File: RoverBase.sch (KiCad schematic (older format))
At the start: 64 parts, among them J1 Conn_01x01, J2 Conn_01x06, J3 Conn_01x04, J4 Conn_01x02, J5 Conn_01x03, J6 Conn_02x03_Counter_Clockwise, J7 Conn_02x03_Counter_Clockwise, J8 Conn_01x01, J9 Conn_01x06, SW1 SW_SPDT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

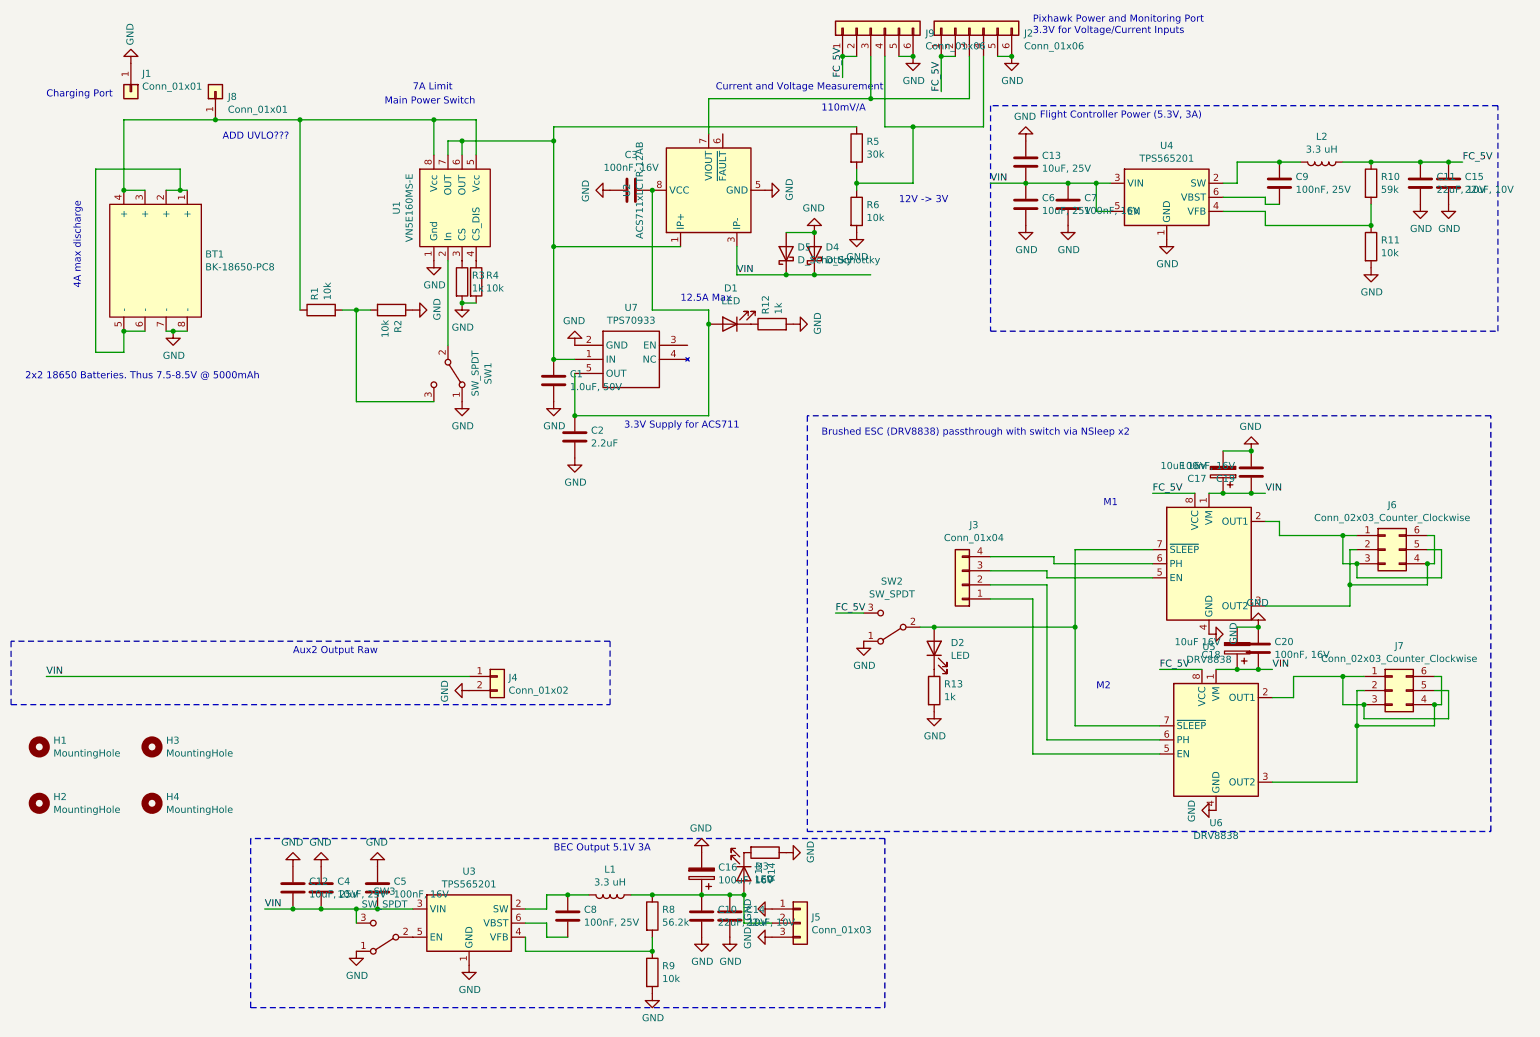
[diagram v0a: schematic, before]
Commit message: Remove diodes and add thermal via for motor controllers
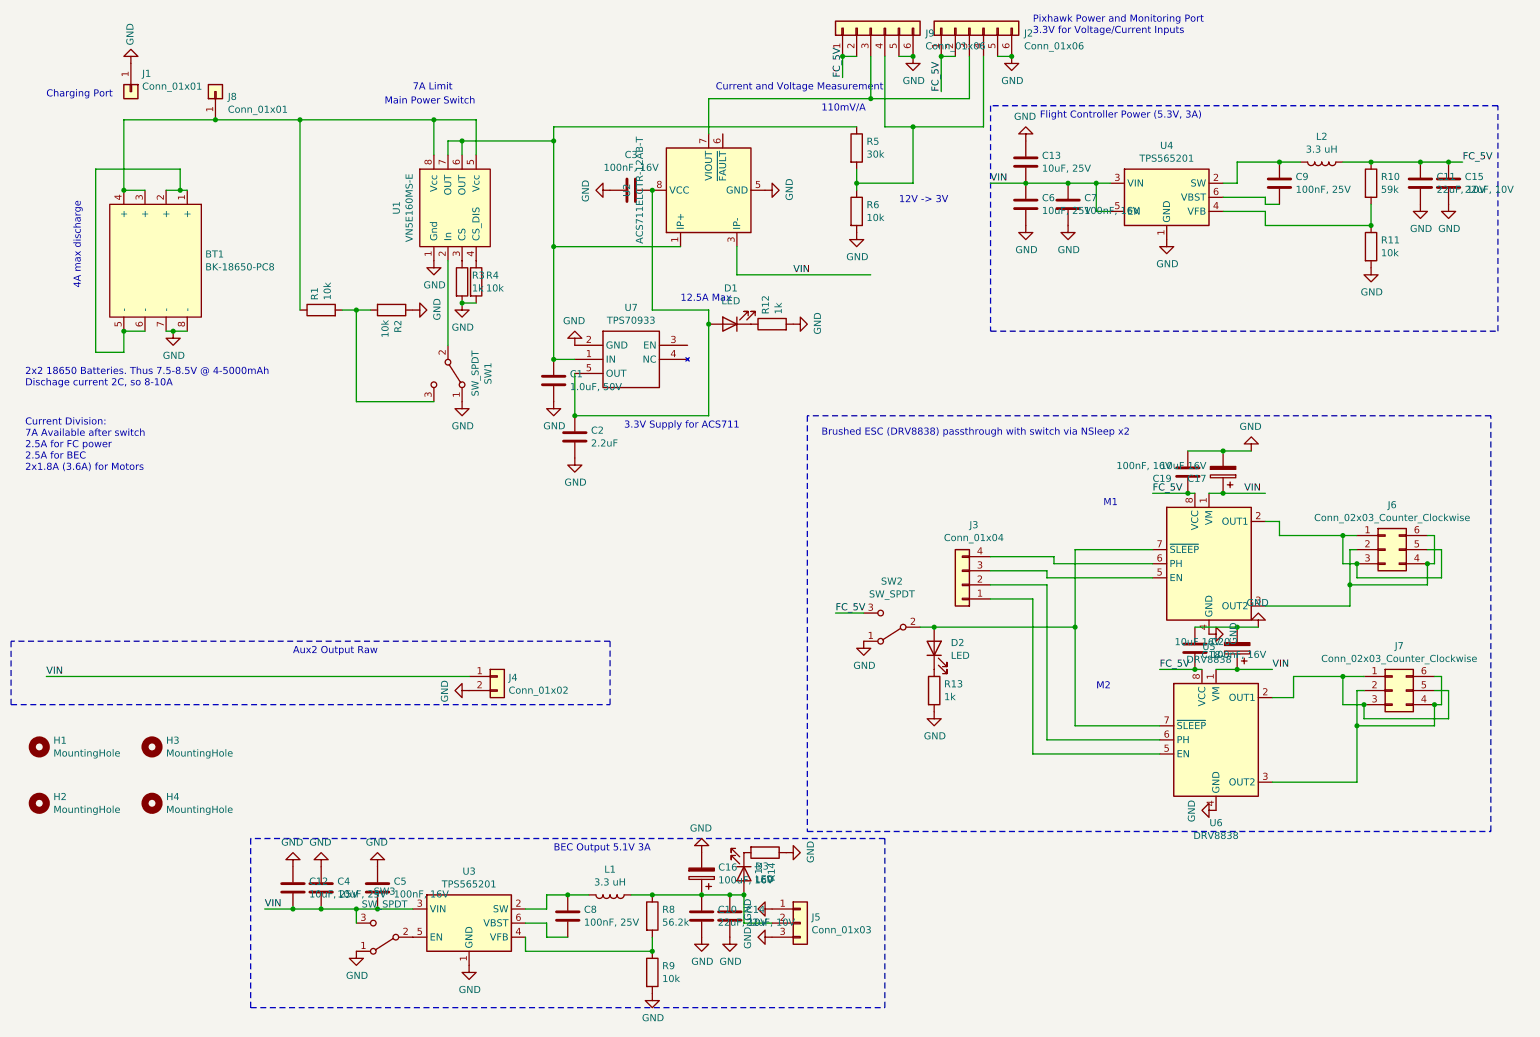
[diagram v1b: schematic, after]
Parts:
- removed D4, D5: D_Schottky, Diode_SMD:D_SOD-323, symbol Device:D_Schottky
- J6, J7: MPN PPPC032LFBN-RC -> nf; Manufacturer Sullins Connector Solutions -> nf; SPN S7106-ND -> nf; fit_field (none) -> dnf
- U2: value ACS711xLCTR-12AB -> ACS711ELCTR-12AB-T
- U5, U6: footprint Package_SON:WSON-8-1EP_2x2mm_P0.5mm_EP0.9x1.6mm -> Package_SON:WSON-8-1EP_2x2mm_P0.5mm_EP0.9x1.6mm_ThermalVias
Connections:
- net FC_5V: now also C19.1, C20.2
- net VIN: no longer C19.1, C20.2
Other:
- note added: "2x2 18650 Batteries. Thus 7.5-8.5V @ 4-5000mAh\nDischage current 2C, so 8-10A\n"
- note added: "Current Division:\n7A Available after switch\n2.5A for FC power\n2.5A for BEC\n2x1.8A (3.6A) for Motors"
- note removed: "2x2 18650 Batteries. Thus 7.5-8.5V @ 5000mAh"
- note removed: "ADD UVLO???"
- moved on the sheet: C19, C20
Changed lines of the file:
@@
 Text Notes 8350 5350 0    50   ~ 0
 M2
-Text Notes 750  3150 0    50   ~ 0
-2x2 18650 Batteries. Thus 7.5-8.5V @ 5000mAh
+Text Notes 750  3200 0    50   ~ 0
+2x2 18650 Batteries. Thus 7.5-8.5V @ 4-5000mAh\nDischage current 2C, so 8-10A\n
 Text Notes 900  1150 0    50   ~ 0
 Charging Port
@@
 P 5600 1800
 F 0 "U2" H 5600 2381 50  0000 C CNN
-F 1 "ACS711xLCTR-12AB" H 5600 2290 50  0000 C CNN
+F 1 "ACS711ELCTR-12AB-T" H 5600 2290 50  0000 C CNN
 F 2 "Package_SO:SOIC-8_3.9x4.9mm_P1.27mm" H 5950 1750 50  0001 L CIN
 F 3 "http://www.allegromicro.com/~/Media/Files/Datasheets/ACS711-Datasheet.ashx" H 5600 1800 50  0001 C CNN
@@
 Text Notes 7950 1300 0    50   ~ 0
 Flight Controller Power (5.3V, 3A)
-Wire Wire Line
-	5800 2400 6150 2400
 Wire Wire Line
 	5800 2200 5800 2400
@@
 	-1   0    0    1
 $EndComp
-Wire Wire Line
-	9550 3950 9450 3950
-Wire Wire Line
-	9600 5200 9500 5200
 Wire Wire Line
 	8450 1950 8350 1950
@@
 F 2 "Connector_PinHeader_2.54mm:PinHeader_2x03_P2.54mm_Vertical" H 10450 5350 50  0001 C CNN
 F 3 "~" H 10450 5350 50  0001 C CNN
-F 4 "PPPC032LFBN-RC" H 10450 5350 50  0001 C CNN "MPN"
-F 5 "S7106-ND" H 10450 5350 50  0001 C CNN "SPN"
-F 6 "Sullins Connector Solutions" H 10450 5350 50  0001 C CNN "Manufacturer"
+F 4 "nf" H 10450 5350 50  0001 C CNN "MPN"
+F 5 "nf" H 10450 5350 50  0001 C CNN "SPN"
+F 6 "nf" H 10450 5350 50  0001 C CNN "Manufacturer"
+F 7 "dnf" H 10450 5350 50  0001 C CNN "fit_field"
 	1    10450 5350
 	1    0    0    -1
@@
 FC_5V
 Wire Wire Line
-	9050 3950 8750 3950
-Wire Wire Line
-	9100 5200 8800 5200
+	9050 3950 9000 3950
+Wire Wire Line
+	9100 5200 9050 5200
 Text Label 8750 3950 0    50   ~ 0
 FC_5V
@@
 Text Label 6500 4800 0    50   ~ 0
 FC_5V
-Text Label 5800 2400 0    50   ~ 0
+Text Label 6200 2400 0    50   ~ 0
 VIN
 Text Label 7600 1750 0    50   ~ 0
 VIN
-Text Label 9550 3950 0    50   ~ 0
+Text Label 9400 3950 0    50   ~ 0
 VIN
 Text Label 9600 5200 0    50   ~ 0
@@
 Wire Wire Line
 	1800 2800 1900 2800
-Text Notes 2150 1450 0    50   ~ 0
-ADD UVLO???
 $Comp
 L Connector_Generic:Conn_02x03_Counter_Clockwise J6
@@
 F 2 "Connector_PinHeader_2.54mm:PinHeader_2x03_P2.54mm_Vertical" H 10400 4350 50  0001 C CNN
 F 3 "~" H 10400 4350 50  0001 C CNN
-F 4 "PPPC032LFBN-RC" H 10400 4350 50  0001 C CNN "MPN"
-F 5 "S7106-ND" H 10400 4350 50  0001 C CNN "SPN"
-F 6 "Sullins Connector Solutions" H 10400 4350 50  0001 C CNN "Manufacturer"
+F 4 "nf" H 10400 4350 50  0001 C CNN "MPN"
+F 5 "nf" H 10400 4350 50  0001 C CNN "SPN"
+F 6 "nf" H 10400 4350 50  0001 C CNN "Manufacturer"
+F 7 "dnf" H 10400 4350 50  0001 C CNN "fit_field"
 	1    10400 4350
 	1    0    0    -1
@@
 	10200 5350 10250 5350
 Connection ~ 10750 5450
-$Comp
-L Device:D_Schottky D4
-U 1 1 5FC09B86
-P 6350 2250
-F 0 "D4" V 6396 2170 50  0000 R CNN
-F 1 "D_Schottky" V 6305 2170 50  0000 R CNN
-F 2 "Diode_SMD:D_SOD-323" H 6350 2250 50  0001 C CNN
-F 3 "~" H 6350 2250 50  0001 C CNN
-F 4 "BAT60AE6327HTSA1" H 6350 2250 50  0001 C CNN "MPN"
-F 5 "BAT60AE6327HTSA1CT-ND" H 6350 2250 50  0001 C CNN "SPN"
-F 6 "Infineon Technologies" H 6350 2250 50  0001 C CNN "Manufacturer"
-	1    6350 2250
-	0    -1   -1   0
-$EndComp
-$Comp
-L power:GND #PWR0102
-U 1 1 5FC12218
-P 6350 2100
-F 0 "#PWR0102" H 6350 1850 50  0001 C CNN
-F 1 "GND" H 6355 1927 50  0000 C CNN
-F 2 "" H 6350 2100 50  0001 C CNN
-F 3 "" H 6350 2100 50  0001 C CNN
-	1    6350 2100
-	-1   0    0    1
-$EndComp
 $Comp
 L Device:CP C16
@@
 	-1   0    0    1
 $EndComp
-Connection ~ 6350 2400
-Wire Wire Line
-	6350 2400 6750 2400
 Wire Wire Line
 	3850 1450 4500 1450
-$Comp
-L Device:D_Schottky D5
-U 1 1 5FC44007
-P 6150 2250
-F 0 "D5" V 6196 2170 50  0000 R CNN
-F 1 "D_Schottky" V 6105 2170 50  0000 R CNN
-F 2 "Diode_SMD:D_SOD-323" H 6150 2250 50  0001 C CNN
-F 3 "~" H 6150 2250 50  0001 C CNN
-F 4 "BAT60AE6327HTSA1" H 6150 2250 50  0001 C CNN "MPN"
-F 5 "BAT60AE6327HTSA1CT-ND" H 6150 2250 50  0001 C CNN "SPN"
-F 6 "Infineon Technologies" H 6150 2250 50  0001 C CNN "Manufacturer"
-	1    6150 2250
-	0    -1   -1   0
-$EndComp
-Connection ~ 6150 2400
-Wire Wire Line
-	6150 2400 6350 2400
-Wire Wire Line
-	6150 2100 6350 2100
-Connection ~ 6350 2100
 Wire Wire Line
 	7200 4900 8200 4900
@@
 F 0 "U5" H 9150 3861 50  0000 C CNN
 F 1 "DRV8838" H 9150 3770 50  0000 C CNN
-F 2 "Package_SON:WSON-8-1EP_2x2mm_P0.5mm_EP0.9x1.6mm" H 9150 3600 50  0001 C CNN
+F 2 "Package_SON:WSON-8-1EP_2x2mm_P0.5mm_EP0.9x1.6mm_ThermalVias" H 9150 3600 50  0001 C CNN
 F 3 "http://www.ti.com/lit/ds/symlink/drv8837.pdf" H 9150 4450 50  0001 C CNN
 F 4 "DRV8838DSGR" H 9150 4450 50  0001 C CNN "MPN"
@@
 F 0 "U6" H 9200 5111 50  0000 C CNN
 F 1 "DRV8838" H 9200 5020 50  0000 C CNN
-F 2 "Package_SON:WSON-8-1EP_2x2mm_P0.5mm_EP0.9x1.6mm" H 9200 4850 50  0001 C CNN
+F 2 "Package_SON:WSON-8-1EP_2x2mm_P0.5mm_EP0.9x1.6mm_ThermalVias" H 9200 4850 50  0001 C CNN
 F 3 "http://www.ti.com/lit/ds/symlink/drv8837.pdf" H 9200 5700 50  0001 C CNN
 F 4 "DRV8838DSGR" H 9200 5700 50  0001 C CNN "MPN"
@@
 L Device:C C19
 U 1 1 6016DF36
-P 9450 3800
-F 0 "C19" H 9565 3846 50  0000 L CNN
-F 1 "100nF, 16V" H 9565 3755 50  0000 L CNN
-F 2 "Capacitor_SMD:C_0402_1005Metric" H 9488 3650 50  0001 C CNN
-F 3 "~" H 9450 3800 50  0001 C CNN
-F 4 "GRM155R71C104KA88D" H 9450 3800 50  0001 C CNN "MPN"
-F 5 "490-3261-1-ND" H 9450 3800 50  0001 C CNN "SPN"
-F 6 "Murata Electronics" H 9450 3800 50  0001 C CNN "Manufacturer"
-	1    9450 3800
+P 9000 3800
+F 0 "C19" H 9115 3846 50  0000 L CNN
+F 1 "100nF, 16V" H 9115 3755 50  0000 L CNN
+F 2 "Capacitor_SMD:C_0402_1005Metric" H 9038 3650 50  0001 C CNN
+F 3 "~" H 9000 3800 50  0001 C CNN
+F 4 "GRM155R71C104KA88D" H 9000 3800 50  0001 C CNN "MPN"
+F 5 "490-3261-1-ND" H 9000 3800 50  0001 C CNN "SPN"
+F 6 "Murata Electronics" H 9000 3800 50  0001 C CNN "Manufacturer"
+	1    9000 3800
 	-1   0    0    1
 $EndComp
@@
 L Device:C C20
 U 1 1 6016EBF6
-P 9500 5050
-F 0 "C20" H 9615 5096 50  0000 L CNN
-F 1 "100nF, 16V" H 9615 5005 50  0000 L CNN
-F 2 "Capacitor_SMD:C_0402_1005Metric" H 9538 4900 50  0001 C CNN
-F 3 "~" H 9500 5050 50  0001 C CNN
-F 4 "GRM155R71C104KA88D" H 9500 5050 50  0001 C CNN "MPN"
-F 5 "490-3261-1-ND" H 9500 5050 50  0001 C CNN "SPN"
-F 6 "Murata Electronics" H 9500 5050 50  0001 C CNN "Manufacturer"
-	1    9500 5050
+P 9050 5050
+F 0 "C20" H 9165 5096 50  0000 L CNN
+F 1 "100nF, 16V" H 9165 5005 50  0000 L CNN
+F 2 "Capacitor_SMD:C_0402_1005Metric" H 9088 4900 50  0001 C CNN
+F 3 "~" H 9050 5050 50  0001 C CNN
+F 4 "GRM155R71C104KA88D" H 9050 5050 50  0001 C CNN "MPN"
+F 5 "490-3261-1-ND" H 9050 5050 50  0001 C CNN "SPN"
+F 6 "Murata Electronics" H 9050 5050 50  0001 C CNN "Manufacturer"
+	1    9050 5050
 	1    0    0    -1
 $EndComp
@@
 Wire Wire Line
 	8000 4600 8000 5700
-Connection ~ 9450 3950
-Wire Wire Line
-	9450 3950 9250 3950
-Connection ~ 9500 5200
-Wire Wire Line
-	9500 5200 9350 5200
 $Comp
 L power:GND #PWR0105
@@
 Wire Wire Line
 	9350 4900 9500 4900
-Connection ~ 9500 4900
 Wire Wire Line
 	9250 3650 9450 3650
-Connection ~ 9450 3650
 $Comp
 L Connector_Generic:Conn_01x06 J9
@@
 Wire Notes Line
 	11150 3400 6300 3400
+Text Notes 750  3800 0    50   ~ 0
+Current Division:\n7A Available after switch\n2.5A for FC power\n2.5A for BEC\n2x1.8A (3.6A) for Motors
+Wire Wire Line
+	5800 2400 6750 2400
+Connection ~ 9000 3950
+Wire Wire Line
+	9000 3950 8750 3950
+Wire Wire Line
+	9250 3950 9550 3950
+Wire Wire Line
+	9000 3650 9250 3650
+Connection ~ 9250 3650
+Connection ~ 9050 5200
+Wire Wire Line
+	9050 5200 8800 5200
+Wire Wire Line
+	9350 5200 9600 5200
+Wire Wire Line
+	9350 4900 9050 4900
+Connection ~ 9350 4900
 $EndSCHEMATC
